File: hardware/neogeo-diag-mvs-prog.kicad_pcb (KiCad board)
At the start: 2 copper layers, 174 x 134 mm, 21 parts, among them J1 NeoGeo MVS Prog B Side Edge, J2 NeoGeo MVS Prog A Side Edge, J3 NeoGeo MVS Prog B Side Edge, J4 NeoGeo MVS Prog A Side Edge, U1 AS6C8016, U2 74LS11, U3 74LS08, U4 74LS04

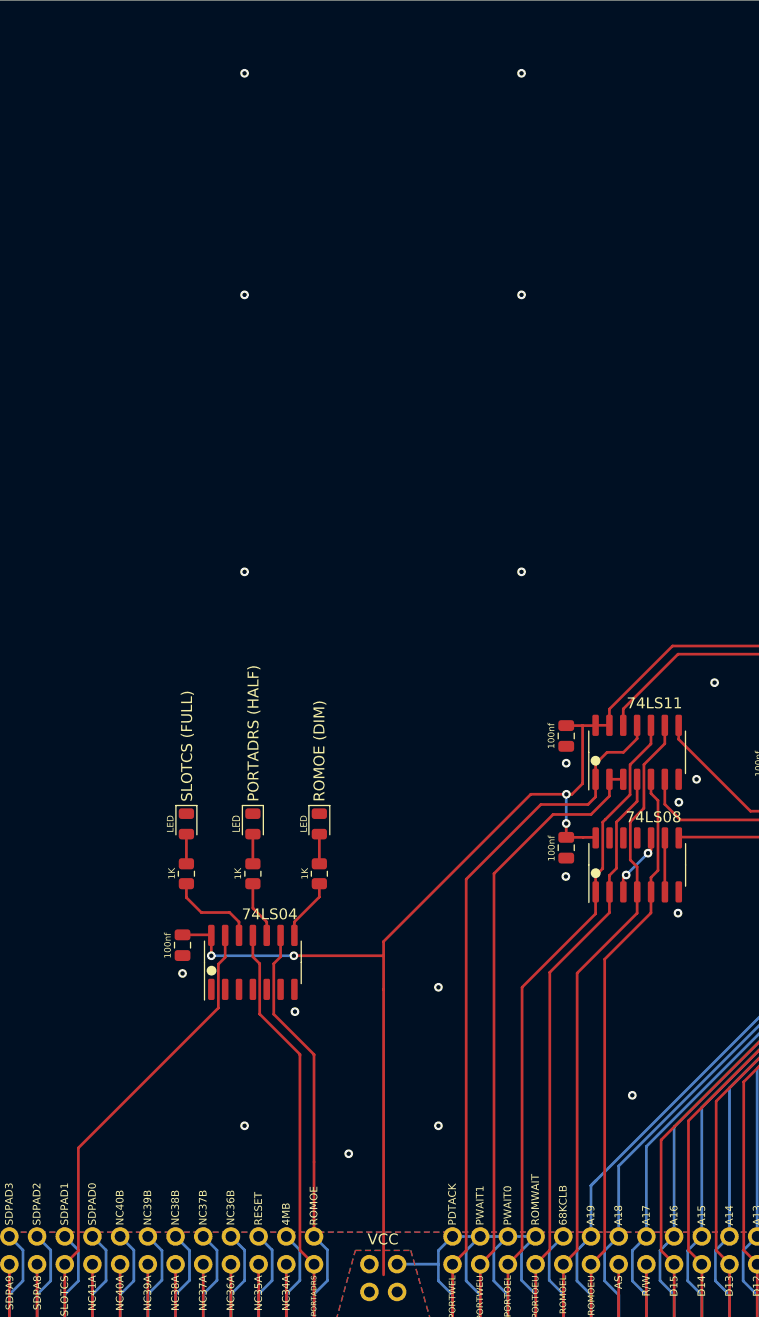
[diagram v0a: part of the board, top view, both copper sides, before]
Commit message: Move leds so they are near the top of the board
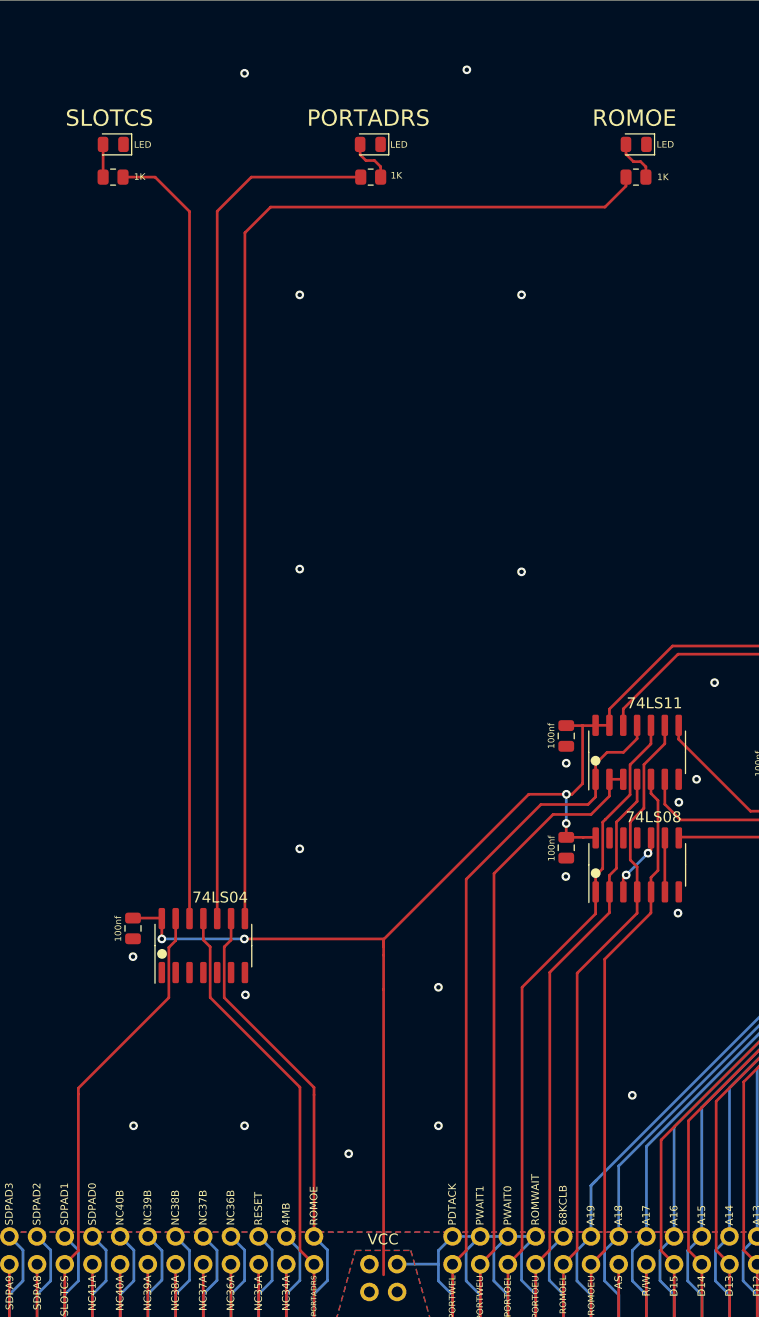
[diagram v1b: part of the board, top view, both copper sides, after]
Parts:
- moved R1 70.2 mm to (162.9, 40.0), turned to 180 degrees
- moved D1 68.8 mm to (162.9, 37.0), turned to 180 degrees
- moved R2 64.8 mm to (138.6, 40.0), turned to 180 degrees
- moved R3 64.2 mm to (115.0, 40.0), turned to 0 degrees
- moved D2 63.2 mm to (138.6, 37.0), turned to 180 degrees
- moved D3 62.7 mm to (115.0, 37.0), turned to 180 degrees
- moved C5 4.79 mm to (116.8, 108.9)
- moved U4 4.79 mm to (123.2, 110.5)
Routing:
- net /!ROMOE: track 5.69 -> 100.4 mm
- net /!PORTADRS: track 5.27 -> 79.3 mm
- net /!SLOTCS: track 8.26 -> 72.2 mm
- net VCC: track 230.8 -> 235.9 mm
- net ROMOE: track 43.5 -> 46.9 mm
- net PORTADRS: track 43.0 -> 46.4 mm
- net Net-(D2-Pad2): track 2.72 -> 4.32 mm
- net Net-(D1-Pad2): track 2.72 -> 4.15 mm
- net GND: vias 49 -> 51
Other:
- board text removed: "PORTADRS (HALF)"
- board text removed: "ROMOE (DIM)"
- board text removed: "SLOTCS (FULL)"

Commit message: Make power traces be 0.5mm, adjustment to some of the text
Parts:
- removed the REF** at (65.5, 39.5) (x2)
- added REF**: OSHW-Logo_11.4x12mm_SilkScreen, Symbol:OSHW-Logo_11.4x12mm_SilkScreen, F.Cu at (66.0, 40.6)
- added REF**: OSHW-Logo_11.4x12mm_SilkScreen, Symbol:OSHW-Logo_11.4x12mm_SilkScreen, B.Cu at (66.0, 40.6)
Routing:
- net VCC: track 235.9 -> 245.2 mm
- net A1: track 63.1 -> 61.4 mm
- net A3: track 58.2 -> 56.5 mm
- net A2: track 60.1 -> 59.0 mm
- net A4: track 55.0 -> 54.1 mm
- net A5: track 52.8 -> 52.0 mm
- net GND: vias 51 -> 52
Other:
- board text added: "LEDS SHOULD BE ON WHEN P ROM BUS TESTS ARE RUNNING"
- board text added: "THIS SIDE OF THE BOARD SHOULD FACE THE PARTS SIDE OF THE CHA BOARD"

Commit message: Add logo
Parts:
- added G***: LOGO, neogeo-diag:neogeo-diag-mvs-prog-logo, F.Cu at (203.2, 39.9)
- added G***: LOGO, neogeo-diag:neogeo-diag-mvs-prog-logo, B.Cu at (203.7, 39.9)
- moved REF** 2.59 mm to (68.6, 40.1) (x2)
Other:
- board text added: "REV ${REV}"
- board text removed: "NEOGEO DIAG MVS PROG ${REV}"
